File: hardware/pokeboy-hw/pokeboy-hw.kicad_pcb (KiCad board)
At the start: 4 copper layers, 79.4 x 119.4 mm, 99 parts, among them J1 USB Micro-B data/power, J2 LiPo 1S + / NTC / -, J3 POWER SWITCH PADS, J4 8 OHM SPEAKER PADS, J5 EA TFT020-23AINN RGB666, J6 UART TEST PADS, J7 RECOVERY SHORT PADS, J8 RESET SHORT PADS, SW1 EVQ-P1905M, SW2 EVQ-P1905M, SW3 EVQ-P1905M, SW4 EVQ-P1905M, SW5 B3AL-1001P, SW6 B3AL-1001P, SW7 EVQ-P2B02B, SW8 EVQ-P2B02B, U1 Core1106, U2 BQ24074RGT, U3 TPS63802DLAR, U4 TPS62162DSG, U5 TPS61165DRV, U6 PAM8302AAD, U7 TPD2EUSB30

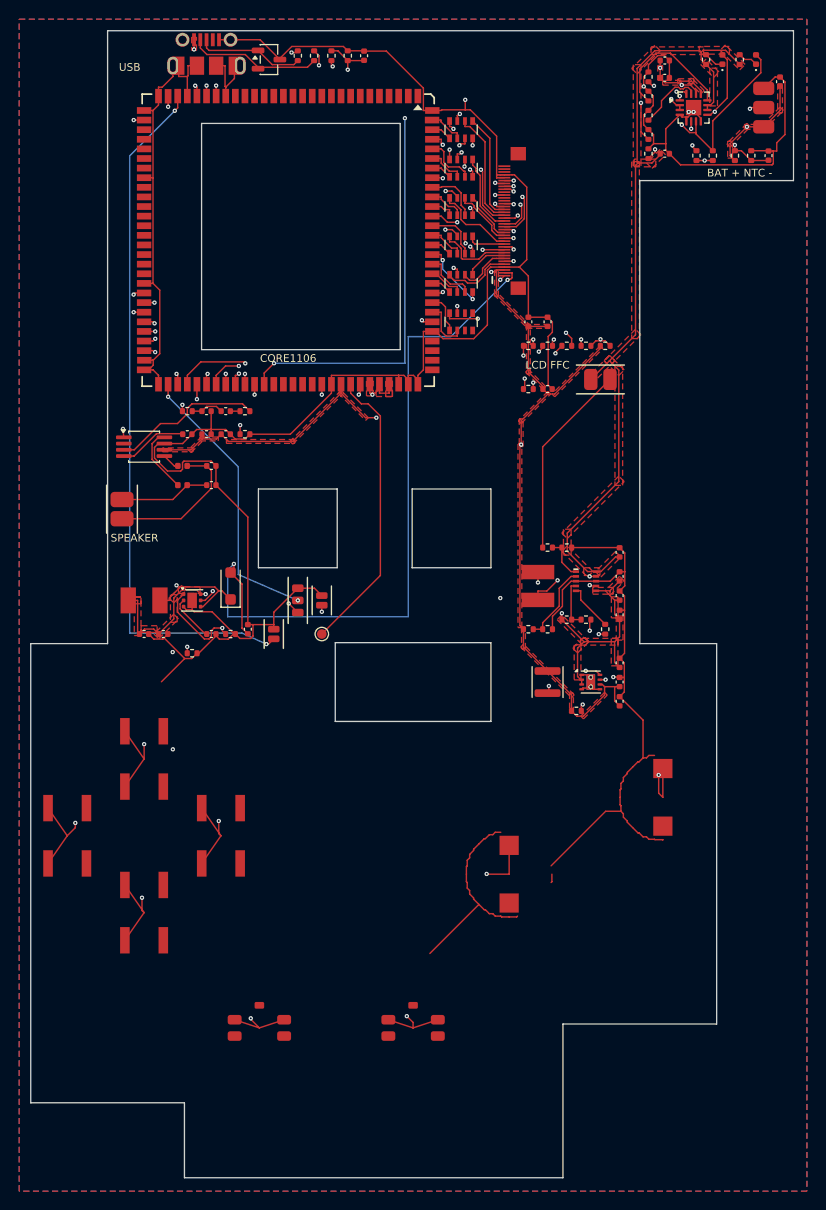
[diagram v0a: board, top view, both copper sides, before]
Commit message: hw: retarget SoM to Octavo OSD3358-1G-ISM (1 GB DDR3L)
Move the main SoM to OSD3358-1G-ISM: 1 GB DDR3L in a 21x21 mm 256-BGA,
1.27 mm pitch, with integrated PMIC. PocketBeagle is the reference design.

- Add Pokeboy.pretty/OSD335X-BGA-256.kicad_mod, adapted from the
  BeagleBoard.org PocketBeagle design (CC BY 4.0); attribution in
  hardware/pokeboy-hw/THIRD_PARTY_NOTICES.md.
- Update schematic, PCB, Core1106 symbol, and the :6767 preview
  renders/FAB_NOTES for the new part.
- Drop the stale PROTO-A fabrication/gerber/source zips. They describe
  the superseded revision and must not be fabricated.

Status: PROTO-B, DFM HOLD. DRC shows no shorts or spacing violations but
still reports 15 unconnected items (SD_D0-D3/SD_CMD/SD_CD_N to the
R104-R109 pullups, OSD_3V3A, SYS_5V, and GND/AUX_3V3 zone islands).
Gerbers are withheld until DRC is clean. Not releasable for fabrication.
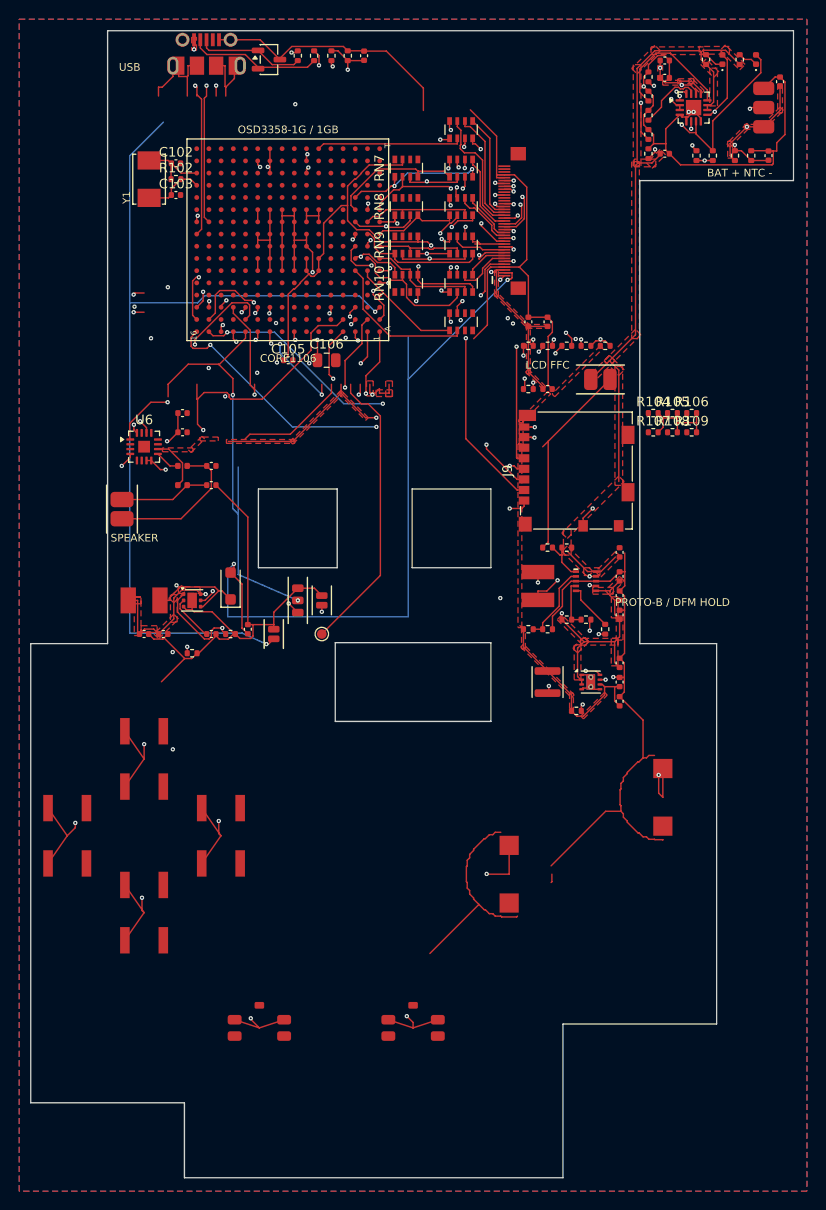
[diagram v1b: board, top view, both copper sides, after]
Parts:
- removed C17, C18, C19: 1u, Capacitor_SMD:C_0402_1005Metric
- removed R24: 100R, Resistor_SMD:R_0402_1005Metric
- removed R25: 33k, Resistor_SMD:R_0402_1005Metric
- removed R26: 100k, Resistor_SMD:R_0402_1005Metric
- added C102: 18pF, C_0402_1005Metric, F.Cu at (15.3, 14.0)
- added C103: 18pF, C_0402_1005Metric, F.Cu at (15.3, 17.3)
- added C105: 100nF, C_0402_1005Metric, F.Cu at (27.0, 34.5)
- added C106: 10uF, C_0805_2012Metric, F.Cu at (31.0, 34.5)
- added J9: 104031-0811, microSD_HC_Molex_104031-0811, F.Cu at (57.0, 46.0)
- added R102: 1M, R_0402_1005Metric, F.Cu at (15.3, 15.7)
- added R104: 10k, R_0402_1005Metric, F.Cu at (65.0, 40.0)
- added R105: 10k, R_0402_1005Metric, F.Cu at (67.0, 40.0)
- added R106: 10k, R_0402_1005Metric, F.Cu at (69.0, 40.0)
- added R107: 10k, R_0402_1005Metric, F.Cu at (65.0, 42.0)
- added R108: 10k, R_0402_1005Metric, F.Cu at (67.0, 42.0)
- added R109: 10k, R_0402_1005Metric, F.Cu at (69.0, 42.0)
- added RN10: 100k, R_Array_Convex_4x0603, F.Cu at (39.3, 26.5)
- added RN7: 100k, R_Array_Convex_4x0603, F.Cu at (39.3, 14.5)
- added RN8: 100k, R_Array_Convex_4x0603, F.Cu at (39.3, 18.5)
- added RN9: 100k, R_Array_Convex_4x0603, F.Cu at (39.3, 22.5)
- added Y1: 24 MHz, PocketBeagle.pretty:CRYSTAL_5X3.2MM, F.Cu at (12.5, 15.7)
- U1: value Core1106 -> OSD3358-1G-ISM; footprint Core1106-PCB:Core1106-SMT -> Pokeboy:OSD335X-BGA-256
- U6: value PAM8302AAD -> MAX98357AETE+T; footprint Package_SO:MSOP-8_3x3mm_P0.65mm -> TQFN-16-1EP_3x3mm_P0.5mm_EP1.23x1.23mm
- moved C21 5.01 mm to (16.0, 40.0)
- moved C20 2.51 mm to (16.0, 42.0)
- turned U1 to 90 degrees
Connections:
- C20 pad 1: /AUX_3V3 -> /SYS_5V
- C21 pad 1: /AUX_3V3 -> /SYS_5V
- U6 pad 1: /AMP_EN -> /I2S_DOUT
- U6 pad 2: unconnected-(U6-NC-Pad2) -> /GND
- U6 pad 3: /AMP_IN_P -> /GND
- U6 pad 4: /AMP_IN_N -> /AMP_EN
- U6 pad 5: /AMP_OUT_P -> (no net)
- U6 pad 6: /AUX_3V3 -> (no net)
- U6 pad 7: /GND -> /SYS_5V
- U6 pad 8: /AMP_OUT_N -> /SYS_5V
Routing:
- net /GND: track 431.1 -> 335.9 mm, vias 6 -> 5
- net /OSD_3V3A: track 0.00 -> 68.8 mm, vias 0 -> 3
- net /SD_CD_N: track 0.00 -> 60.1 mm, vias 0 -> 3
- net /SD_D2: track 0.00 -> 57.2 mm, vias 0 -> 3
- net /SD_CMD: track 0.00 -> 53.8 mm, vias 0 -> 3
- net /OSD_3V3B: track 0.00 -> 50.6 mm, vias 0 -> 2
- net /SD_CLK: track 0.00 -> 49.2 mm, vias 0 -> 2
- net /SD_D3: track 0.00 -> 48.1 mm, vias 0 -> 2
- net /AUX_3V3: track 149.8 -> 104.3 mm, vias 5 -> 4
- net /SYS_5V: track 103.4 -> 148.5 mm, vias 3 -> 9
- net /SD_D0: track 0.00 -> 42.9 mm, vias 0 -> 3
- net /SD_D1: track 0.00 -> 39.6 mm, vias 0 -> 3
- net /I2S_DOUT: track 0.00 -> 33.7 mm, vias 0 -> 2
- net /I2S_BCLK: track 0.00 -> 33.6 mm, vias 0 -> 2
- net /CODEC_LINEOUT: track 33.5 -> 0.00 mm, vias 2 -> 0
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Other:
- outline, holes or cut-outs redrawn
- board text added: "OSD3358-1G / 1GB"
- board text added: "PROTO-B / DFM HOLD"

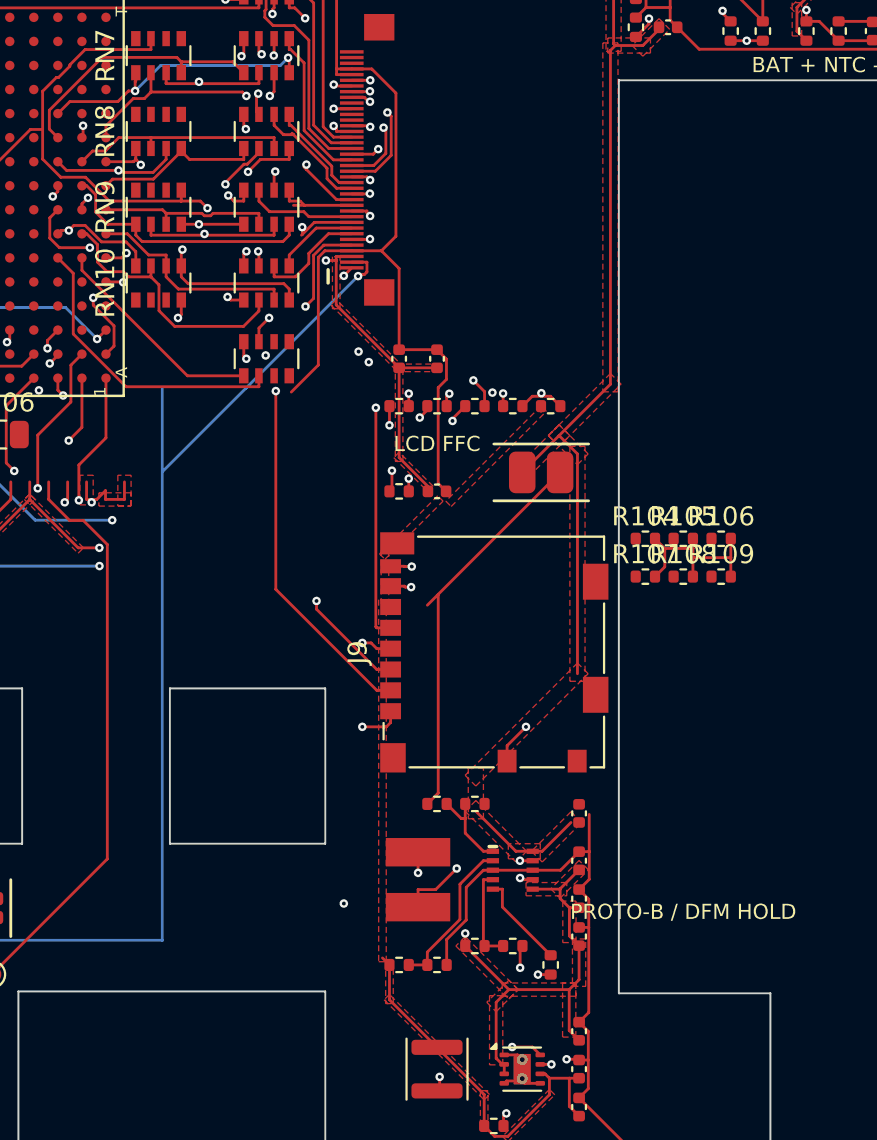
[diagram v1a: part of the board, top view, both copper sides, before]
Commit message: hw: bring the SD pull-ups on-board and repair the 3V3 / GND nets
DRC reported 15 unconnected items. The root cause of 7 of them was not
routing: R104-R109 (the microSD signal pull-ups) and their OSD_3V3A rail
were placed past the board outline, which steps in to x=63.6 mm for
y>15.8 mm. All 12 pads and 20 rail endpoints were off-board, so those
nets could not be routed at all.

- Relocate R104-R109 into the open pocket between the U1 escape and J9
  (2 columns x 3 rows at x=46.6/49.0, y=33.8/35.5/37.2), and match the
  board's silkscreen convention for 0402s (reference/value hidden).
- Route all six signals: F.Cu stubs into via corridors between the
  In1 tracks, then B.Cu (previously empty in this region) to verified
  via sites on each net. Rebuild the OSD_3V3A rail on F.Cu and tie it
  to the existing In2 spine at x=49.858.
- Delete the stale off-board OSD_3V3A tracks.

AUX_3V3 was in four disconnected components: U4/L2 generate 3V3 but it
reached neither J5, the C24/C25/C26 decoupling, U2, nor R31. Join them
with three 0.40 mm B.Cu links plus a short F.Cu link into C26 pad 1.

Also stitch three orphaned F.Cu GND pour islands to the ground planes,
and bridge the SYS_5V island feeding U6/C20/C21 to the main rail on In1.

Regenerate CPL.csv, DFM_DRC_REPORT.txt, the copper plots and the board
renders from this board. The schematic and netlist are unchanged.

DRC: 15 unconnected -> 1, warnings 99 -> 81, still zero shorts/spacing
errors. Board remains PROTO-B / DFM HOLD and Gerbers stay withheld.

Still open: RN10 pad 3, the SYSBOOT pull-down ground for LCD_D2_CORE.
Its pour island is pinched off by the LCD_D1_CORE escape at x=39.323 mm
and the surrounding LCD_D1/D2/D3_CORE and OSD_3V3B routing leaves no via
site with usable clearance; the only DRC-legal option is a via in the pad
at ~0.008 mm margin. Closing it needs a local re-layout, and until then
the LCD_D2_CORE SYSBOOT strap floats at reset.
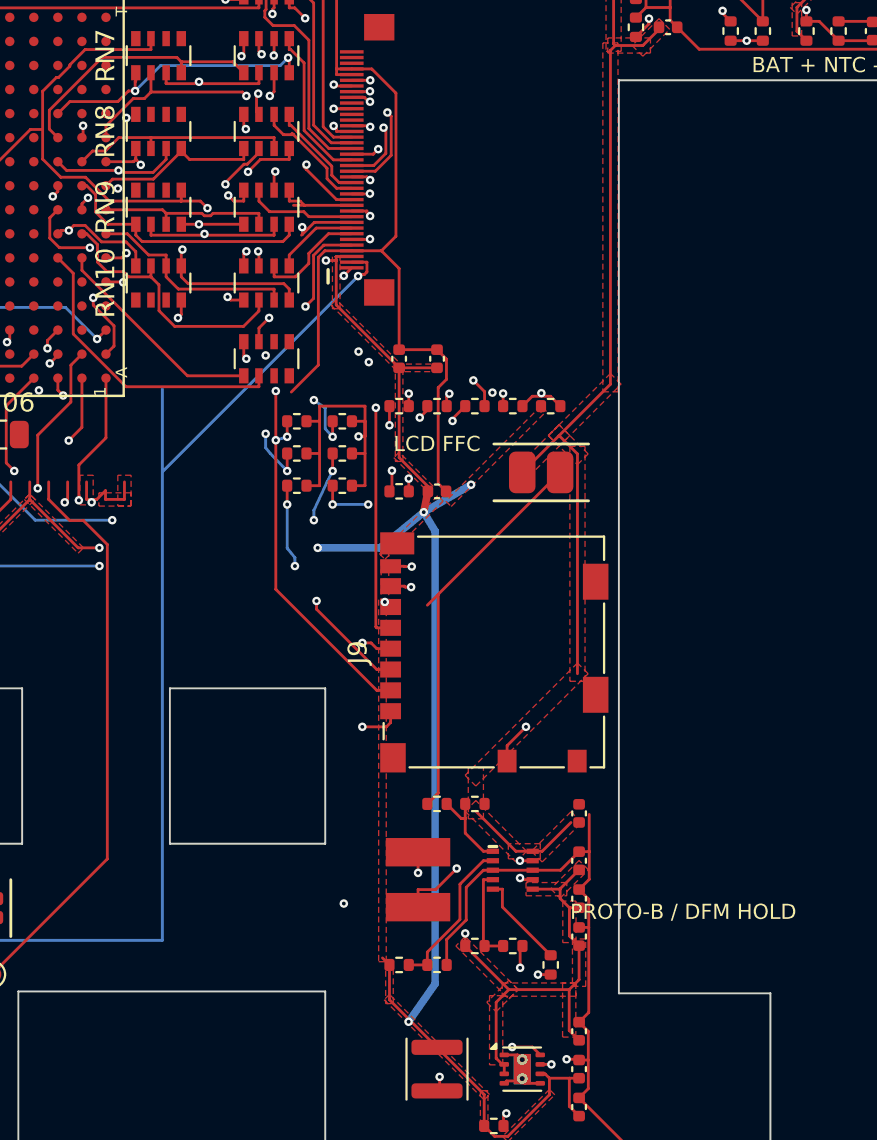
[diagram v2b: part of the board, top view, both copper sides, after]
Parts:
- moved R109 21.6 mm to (49.0, 33.8)
- moved R108 21.4 mm to (46.6, 35.5)
- moved R106 20.2 mm to (49.0, 37.2)
- moved R107 20.1 mm to (46.6, 33.8)
- moved R104 18.6 mm to (46.6, 37.2)
- moved R105 18.6 mm to (49.0, 35.5)
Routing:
- net /AUX_3V3: track 104.3 -> 142.0 mm, vias 4 -> 8
- net /SYS_5V: track 148.5 -> 170.0 mm
- net /OSD_3V3A: track 68.8 -> 74.9 mm, vias 3 -> 4
- net /SD_D0: track 42.9 -> 47.2 mm, vias 3 -> 5
- net /SD_D1: track 39.6 -> 43.3 mm, vias 3 -> 5
- net /SD_CMD: track 53.8 -> 57.2 mm, vias 3 -> 5
- net /SD_CD_N: track 60.1 -> 63.4 mm, vias 3 -> 5
- net /SD_D2: track 57.2 -> 60.1 mm, vias 3 -> 5
- net /SD_D3: track 48.1 -> 49.6 mm, vias 2 -> 4
- net /GND: vias 5 -> 8

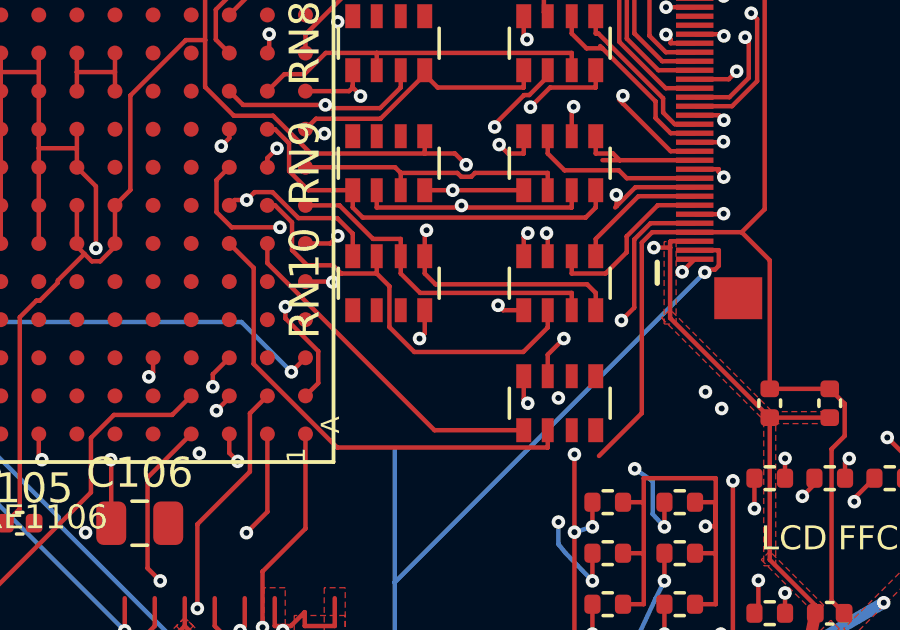
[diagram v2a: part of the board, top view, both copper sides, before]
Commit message: hw: reroute LCD_D1_CORE out of the RN10 pad gap - DRC now clean
The last unconnected item was RN10 pad 3, the SYSBOOT pull-down ground
for LCD_D2_CORE. Its F.Cu pour island had no room for a stitching via:
the island is walled by the LCD_D1_CORE escape at x=39.323 and the
OSD_3V3B In2 spine at x=40.158, a 0.835 mm corridor where a 0.45 mm via
needs 0.800 mm. Widening it eastward is blocked by the LCD_D3_CORE via
at (40.560,24.735), and pad 3 is only 0.4 mm wide, so any via there
protrudes past the pad.

Fix the cause instead of the symptom. LCD_D1_CORE ran from RN10 pad 7
south through the 0.4 mm gap between pads 2 and 3 - both GND - which is
what pinched the pour off. Move that branch off F.Cu:

- Drop the three F.Cu segments threading the pad gap.
- Escape to B.Cu at (39.100,26.400) clear of the gap, run 3.4 mm under
  the array on B.Cu (empty there), and rejoin the original F.Cu line
  with a via at (41.500,28.792).

With the gap clear the GND pour merges pads 2 and 3 by itself, so no
stitching via is needed. Via margins are 0.135 mm and 0.091 mm.
LCD_D1_CORE remains U1.G2 -> RN10.7 -> RN1.2.

DRC: 0 errors, 0 unconnected (was 15). ERC: clean. Warnings 99 -> 81,
every category at or below the previous board.

The DRC/ERC release gate is now met. Gerbers stay withheld and the
package stays DFM HOLD: Octavo's OSD335x design review is the open gate
and has not been done. Docs updated to say so rather than citing DRC.

Regenerate the DRC report, copper plots and renders. CPL is unchanged -
no parts moved. Schematic and netlist unchanged.
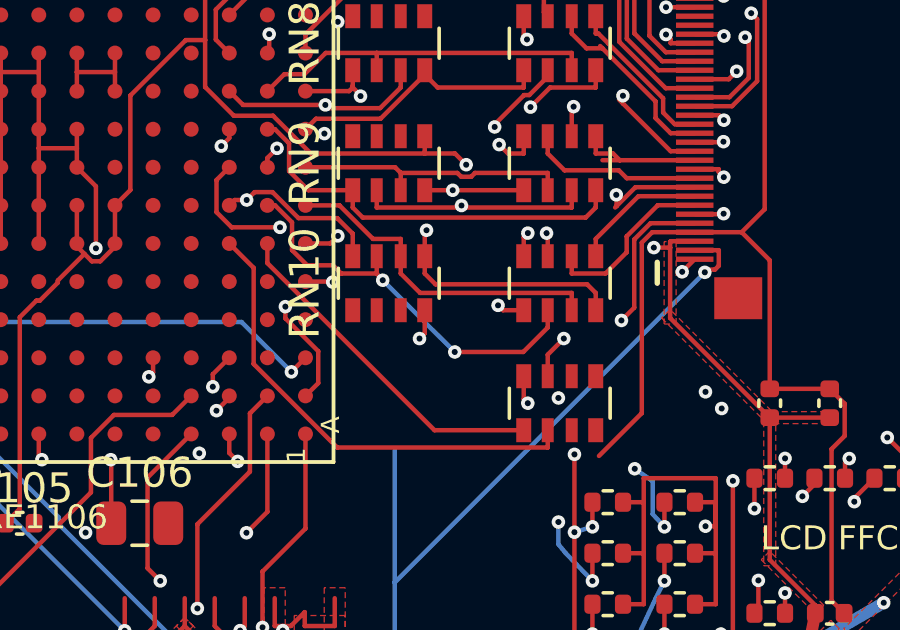
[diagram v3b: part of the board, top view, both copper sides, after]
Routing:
- net /LCD_D1_CORE: track 14.2 -> 13.4 mm, vias 0 -> 2
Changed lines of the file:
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@@
 	)
 	(segment
-		(start 39.3233 26.6)
-		(end 38.9 26.1767)
+		(start 38.9 26.177)
+		(end 39.1 26.4)
 		(width 0.15)
 		(layer "F.Cu")
@@
 	)
 	(segment
-		(start 39.3233 27.9632)
-		(end 39.3233 26.6)
-		(width 0.15)
-		(layer "F.Cu")
-		(net 57)
-	)
-	(segment
 		(start 38.9 25.6)
 		(end 38.9 26.1767)
@@
 	)
 	(segment
-		(start 40.1522 28.7921)
-		(end 39.3233 27.9632)
-		(width 0.15)
-		(layer "F.Cu")
-		(net 57)
-	)
-	(segment
 		(start 43.7846 28.7921)
-		(end 40.1522 28.7921)
+		(end 41.5 28.792)
 		(width 0.15)
 		(layer "F.Cu")
@@
 		(net 57)
 	)
+	(via
+		(at 39.1 26.4)
+		(size 0.45)
+		(drill 0.2)
+		(layers "F.Cu" "B.Cu")
+		(net 57)
+	)
+	(via
+		(at 41.5 28.792)
+		(size 0.45)
+		(drill 0.2)
+		(layers "F.Cu" "B.Cu")
+		(net 57)
+	)
+	(segment
+		(start 39.1 26.4)
+		(end 41.5 28.792)
+		(width 0.15)
+		(layer "B.Cu")
+		(net 57)
+	)
